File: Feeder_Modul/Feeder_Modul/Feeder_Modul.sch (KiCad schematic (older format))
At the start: 99 parts, among them J1 Conn_02x01, J101 Conn_02x01, J102 Conn_01x06_Male, J103 Conn_02x01, J104 Conn_02x01, J105 Conn_02x01, J106 USB_A, J107 Conn_02x07_Odd_Even, J108 Conn_02x01, J109 Conn_02x01, Q101 BC847, SW101 SW_Push, SW102 SW_Push, SW103 SW_Push, SW104 SW_Push, SW105 SW_Push, U1 TPS560430, U101 TPS560430, U102 STM32F105R8Tx, U103 M24C01-WMN, U104 EE-SX1350_PCB, U105 DRV8835, U107 SN65HVD230, Y101 48MHz

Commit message: Controller Modul geroutet
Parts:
- removed Q101: BC847, Package_TO_SOT_SMD:SOT-23, symbol Transistor_BJT:BC847
- removed R116: 10K, Resistor_SMD:R_0603_1608Metric, symbol Device:R_Small
- added D105: LED_Blue, LED_SMD:LED_0603_1608Metric, symbol Device:LED_Small
- J106: value USB_A -> WE_629104190121; footprint ProjectFootprints:USB-A-Conn_LCSC -> ProjectFootprints:WE629104190121; LCSC C46405 -> (none)
- R113: value 10K -> 1K; LCSC C99198 -> C21190
- R115: value 1k -> 10K; LCSC C21190 -> C99198
- U104: value EE-SX1350_PCB -> TCST5250; footprint ProjectFootprints:EE-SX1350_90deg -> ProjectFootprints:TCST5250; symbol PorjectLibrary:EE-SX1350_PCB -> PorjectLibrary:TCST5250
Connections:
- net +3V3: now also R115.2, D105.2 (A); no longer U104.4 (C)
- net ENC_OUT: now also R113.1, R115.1, U104.4 (C)
- net GND: now also U104.2 (C); no longer R113.2
- new net: D105.1 (K), R113.2
- no-connect marks 23 -> 21
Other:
- moved on the sheet: R109, R113
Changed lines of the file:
@@
 Connection ~ 14700 3400
 $Comp
-L PorjectLibrary:EE-SX1350_PCB U104
+L PorjectLibrary:TCST5250 U104
 U 1 1 60136449
-P 9400 4750
-F 0 "U104" H 9225 5147 60  0000 C CNN
-F 1 "EE-SX1350_PCB" H 9225 5041 60  0000 C CNN
-F 2 "ProjectFootprints:EE-SX1350_90deg" H 9400 4750 60  0001 C CNN
-F 3 "https://www.mouser.de/datasheet/2/307/en-ee_sx1350-1076544.pdf" H 9400 4750 60  0001 C CNN
-	1    9400 4750
-	1    0    0    -1
-$EndComp
-$Comp
-L Transistor_BJT:BC847 Q101
-U 1 1 6013824A
-P 10400 4600
-F 0 "Q101" H 10591 4646 50  0000 L CNN
-F 1 "BC847" H 10591 4555 50  0000 L CNN
-F 2 "Package_TO_SOT_SMD:SOT-23" H 10600 4525 50  0001 L CIN
-F 3 "http://www.infineon.com/dgdl/Infineon-BC847SERIES_BC848SERIES_BC849SERIES_BC850SERIES-DS-v01_01-en.pdf?fileId=db3a304314dca389011541d4630a1657" H 10400 4600 50  0001 L CNN
-F 4 "C475630" H 10750 4450 50  0000 C CNN "LCSC"
-	1    10400 4600
-	1    0    0    -1
-$EndComp
-$Comp
-L Device:R_Small R113
-U 1 1 60138354
-P 9850 4300
-F 0 "R113" H 9791 4254 50  0000 R CNN
-F 1 "10K" H 9791 4345 50  0000 R CNN
-F 2 "Resistor_SMD:R_0603_1608Metric" H 9850 4300 50  0001 C CNN
-F 3 "~" H 9850 4300 50  0001 C CNN
-F 4 "C99198" H 9850 4300 50  0001 C CNN "LCSC"
-	1    9850 4300
-	-1   0    0    1
-$EndComp
-Wire Wire Line
-	9850 4400 9850 4600
-$Comp
-L Device:R_Small R115
-U 1 1 6013AC18
-P 10100 4600
-F 0 "R115" V 9904 4600 50  0000 C CNN
-F 1 "1k" V 9995 4600 50  0000 C CNN
-F 2 "Resistor_SMD:R_0603_1608Metric" H 10100 4600 50  0001 C CNN
-F 3 "~" H 10100 4600 50  0001 C CNN
-F 4 "C21190" H 10100 4600 50  0001 C CNN "LCSC"
-	1    10100 4600
-	0    1    1    0
-$EndComp
-$Comp
-L power:GND #PWR0134
-U 1 1 6013AD13
-P 9850 4200
-F 0 "#PWR0134" H 9850 3950 50  0001 C CNN
-F 1 "GND" H 9855 4027 50  0000 C CNN
-F 2 "" H 9850 4200 50  0001 C CNN
-F 3 "" H 9850 4200 50  0001 C CNN
-	1    9850 4200
-	-1   0    0    1
-$EndComp
-Connection ~ 9850 4600
-Wire Wire Line
-	9850 4600 9700 4600
-Wire Wire Line
-	9850 4600 10000 4600
-$Comp
-L power:+3V3 #PWR0135
-U 1 1 601423FC
-P 9850 4900
-F 0 "#PWR0135" H 9850 4750 50  0001 C CNN
-F 1 "+3V3" V 9865 5028 50  0000 L CNN
-F 2 "" H 9850 4900 50  0001 C CNN
-F 3 "" H 9850 4900 50  0001 C CNN
-	1    9850 4900
-	0    1    1    0
-$EndComp
-Wire Wire Line
-	9850 4900 9700 4900
-$Comp
-L power:GND #PWR0138
-U 1 1 60144C45
-P 10500 5050
-F 0 "#PWR0138" H 10500 4800 50  0001 C CNN
-F 1 "GND" H 10505 4877 50  0000 C CNN
-F 2 "" H 10500 5050 50  0001 C CNN
-F 3 "" H 10500 5050 50  0001 C CNN
-	1    10500 5050
-	1    0    0    -1
-$EndComp
-Wire Wire Line
-	10500 5050 10500 4800
+P 8200 5250
+F 0 "U104" H 8025 5647 60  0000 C CNN
+F 1 "TCST5250" H 8025 5541 60  0000 C CNN
+F 2 "ProjectFootprints:TCST5250" H 8200 5250 60  0001 C CNN
+F 3 "https://www.mouser.de/datasheet/2/307/en-ee_sx1350-1076544.pdf" H 8200 5250 60  0001 C CNN
+	1    8200 5250
+	1    0    0    -1
+$EndComp
+Wire Wire Line
+	6950 4450 6950 4650
 $Comp
 L power:+3V3 #PWR0137
 U 1 1 6014609C
-P 10500 4000
-F 0 "#PWR0137" H 10500 3850 50  0001 C CNN
-F 1 "+3V3" H 10515 4173 50  0000 C CNN
-F 2 "" H 10500 4000 50  0001 C CNN
-F 3 "" H 10500 4000 50  0001 C CNN
-	1    10500 4000
-	1    0    0    -1
-$EndComp
-$Comp
-L Device:R_Small R116
-U 1 1 6014615D
-P 10500 4100
-F 0 "R116" H 10441 4054 50  0000 R CNN
-F 1 "10K" H 10441 4145 50  0000 R CNN
-F 2 "Resistor_SMD:R_0603_1608Metric" H 10500 4100 50  0001 C CNN
-F 3 "~" H 10500 4100 50  0001 C CNN
-F 4 "C99198" H 10500 4100 50  0001 C CNN "LCSC"
-	1    10500 4100
-	-1   0    0    1
-$EndComp
-Wire Wire Line
-	10500 4200 10500 4300
-Text Label 10650 4300 0    50   ~ 0
+P 6950 4050
+F 0 "#PWR0137" H 6950 3900 50  0001 C CNN
+F 1 "+3V3" H 6965 4223 50  0000 C CNN
+F 2 "" H 6950 4050 50  0001 C CNN
+F 3 "" H 6950 4050 50  0001 C CNN
+	1    6950 4050
+	-1   0    0    -1
+$EndComp
+Text Label 6700 4650 2    50   ~ 0
 ENC_OUT
-Wire Wire Line
-	10650 4300 10500 4300
-Connection ~ 10500 4300
-Wire Wire Line
-	10500 4300 10500 4400
 $Comp
 L Device:R_Small R109
 U 1 1 6014909F
-P 8400 4600
-F 0 "R109" V 8204 4600 50  0000 C CNN
-F 1 "1k" V 8295 4600 50  0000 C CNN
-F 2 "Resistor_SMD:R_0603_1608Metric" H 8400 4600 50  0001 C CNN
-F 3 "~" H 8400 4600 50  0001 C CNN
-F 4 "C21190" H 8400 4600 50  0001 C CNN "LCSC"
-	1    8400 4600
+P 7850 4000
+F 0 "R109" V 7654 4000 50  0000 C CNN
+F 1 "1k" V 7745 4000 50  0000 C CNN
+F 2 "Resistor_SMD:R_0603_1608Metric" H 7850 4000 50  0001 C CNN
+F 3 "~" H 7850 4000 50  0001 C CNN
+F 4 "C21190" H 7850 4000 50  0001 C CNN "LCSC"
+	1    7850 4000
 	0    1    1    0
 $EndComp
 Wire Wire Line
-	8750 4600 8500 4600
+	8000 4000 7950 4000
 $Comp
 L power:+3V3 #PWR0129
 U 1 1 6014A83A
-P 8050 4600
-F 0 "#PWR0129" H 8050 4450 50  0001 C CNN
-F 1 "+3V3" V 8065 4728 50  0000 L CNN
-F 2 "" H 8050 4600 50  0001 C CNN
-F 3 "" H 8050 4600 50  0001 C CNN
-	1    8050 4600
-	0    -1   -1   0
-$EndComp
-Wire Wire Line
-	8300 4600 8050 4600
+P 7700 3550
+F 0 "#PWR0129" H 7700 3400 50  0001 C CNN
+F 1 "+3V3" V 7715 3678 50  0000 L CNN
+F 2 "" H 7700 3550 50  0001 C CNN
+F 3 "" H 7700 3550 50  0001 C CNN
+	1    7700 3550
+	1    0    0    -1
+$EndComp
+Wire Wire Line
+	7750 4000 7700 4000
 $Comp
 L power:GND #PWR0128
 U 1 1 6014C039
-P 8000 4900
-F 0 "#PWR0128" H 8000 4650 50  0001 C CNN
-F 1 "GND" V 8005 4772 50  0000 R CNN
-F 2 "" H 8000 4900 50  0001 C CNN
-F 3 "" H 8000 4900 50  0001 C CNN
-	1    8000 4900
+P 7750 4150
+F 0 "#PWR0128" H 7750 3900 50  0001 C CNN
+F 1 "GND" V 7900 4150 50  0000 R CNN
+F 2 "" H 7750 4150 50  0001 C CNN
+F 3 "" H 7750 4150 50  0001 C CNN
+	1    7750 4150
 	0    1    1    0
 $EndComp
-Wire Wire Line
-	8750 4900 8000 4900
-NoConn ~ 8750 4750
-NoConn ~ 9700 4750
 Text Notes 14350 8350 0    50   ~ 0
 Feeder Steckplatz
@@
 P 14500 6100
 F 0 "J106" H 14555 6567 50  0000 C CNN
-F 1 "USB_A" H 14555 6476 50  0000 C CNN
-F 2 "ProjectFootprints:USB-A-Conn_LCSC" H 14650 6050 50  0001 C CNN
+F 1 "WE_629104190121" H 14555 6476 50  0000 C CNN
+F 2 "ProjectFootprints:WE629104190121" H 14650 6050 50  0001 C CNN
 F 3 "https://datasheet.lcsc.com/szlcsc/1811170208_Jing-Extension-of-the-Electronic-Co-LCSC-A-F90-Vinyl-Not-high-temperature_C46405.pdf" H 14650 6050 50  0001 C CNN
-F 4 "C46405" H 14550 6650 50  0000 C CNN "LCSC"
 	1    14500 6100
 	-1   0    0    -1
@@
 Text Notes 9100 5400 0    50   ~ 0
 Vishay Semiconductors\nCST5250
+Wire Wire Line
+	7700 3550 7700 4000
+Wire Wire Line
+	8000 4150 7750 4150
+$Comp
+L power:GND #PWR0134
+U 1 1 604E036D
+P 6700 4750
+F 0 "#PWR0134" H 6700 4500 50  0001 C CNN
+F 1 "GND" V 6705 4622 50  0000 R CNN
+F 2 "" H 6700 4750 50  0001 C CNN
+F 3 "" H 6700 4750 50  0001 C CNN
+	1    6700 4750
+	0    1    1    0
+$EndComp
+Wire Wire Line
+	6700 4750 8000 4750
+$Comp
+L Device:R_Small R113
+U 1 1 60138354
+P 6950 4350
+F 0 "R113" H 7250 4300 50  0000 R CNN
+F 1 "1K" H 7150 4400 50  0000 R CNN
+F 2 "Resistor_SMD:R_0603_1608Metric" H 6950 4350 50  0001 C CNN
+F 3 "~" H 6950 4350 50  0001 C CNN
+F 4 "C21190" H 6950 4350 50  0001 C CNN "LCSC"
+	1    6950 4350
+	1    0    0    1
+$EndComp
+Wire Wire Line
+	6950 4650 6800 4650
+Connection ~ 6950 4650
+$Comp
+L Device:LED_Small D105
+U 1 1 60570A78
+P 6950 4150
+F 0 "D105" V 7000 3950 50  0000 C CNN
+F 1 "LED_Blue" V 6900 3850 50  0000 C CNN
+F 2 "LED_SMD:LED_0603_1608Metric" V 6950 4150 50  0001 C CNN
+F 3 "https://datasheet.lcsc.com/szlcsc/TOGIALED-TJ-S1608SW6TGLC6B-A5_C192317.pdf" V 6950 4150 50  0001 C CNN
+F 4 "C192317" H 6950 4150 50  0001 C CNN "LCSC"
+	1    6950 4150
+	0    -1   -1   0
+$EndComp
+Wire Wire Line
+	6950 4650 8000 4650
+$Comp
+L Device:R_Small R115
+U 1 1 6017D48A
+P 6800 4350
+F 0 "R115" H 6741 4304 50  0000 R CNN
+F 1 "10K" H 6741 4395 50  0000 R CNN
+F 2 "Resistor_SMD:R_0603_1608Metric" H 6800 4350 50  0001 C CNN
+F 3 "~" H 6800 4350 50  0001 C CNN
+F 4 "C99198" H 6800 4350 50  0001 C CNN "LCSC"
+	1    6800 4350
+	1    0    0    1
+$EndComp
+Wire Wire Line
+	6800 4250 6800 4050
+Wire Wire Line
+	6800 4050 6950 4050
+Connection ~ 6950 4050
+Wire Wire Line
+	6800 4450 6800 4650
+Connection ~ 6800 4650
+Wire Wire Line
+	6800 4650 6700 4650
 $EndSCHEMATC

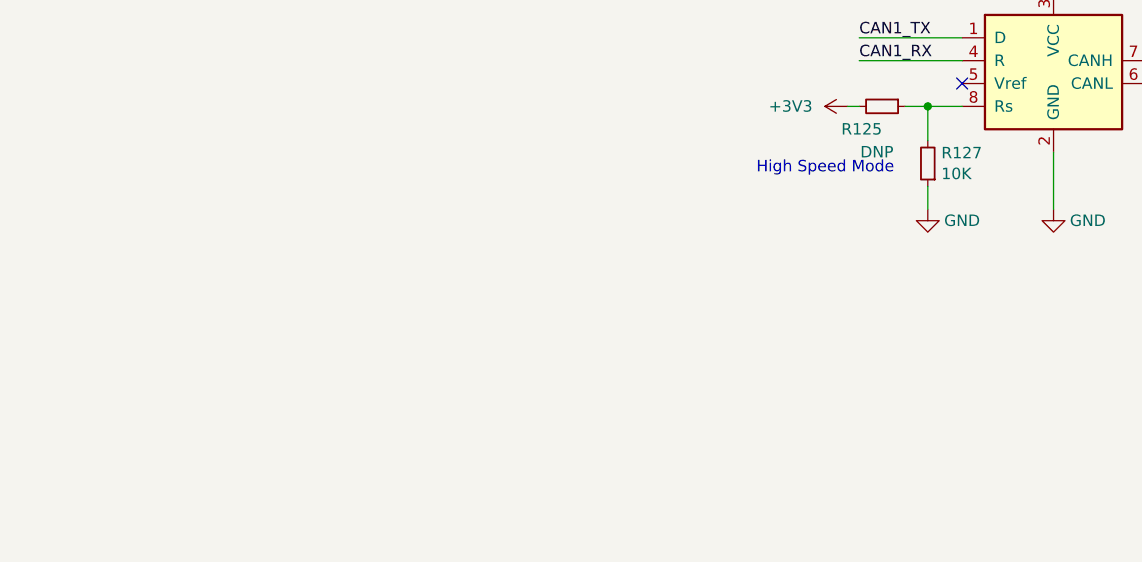
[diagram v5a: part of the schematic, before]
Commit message: Leere Symbole mit leeren Footprints hinzugefügt für BOM export
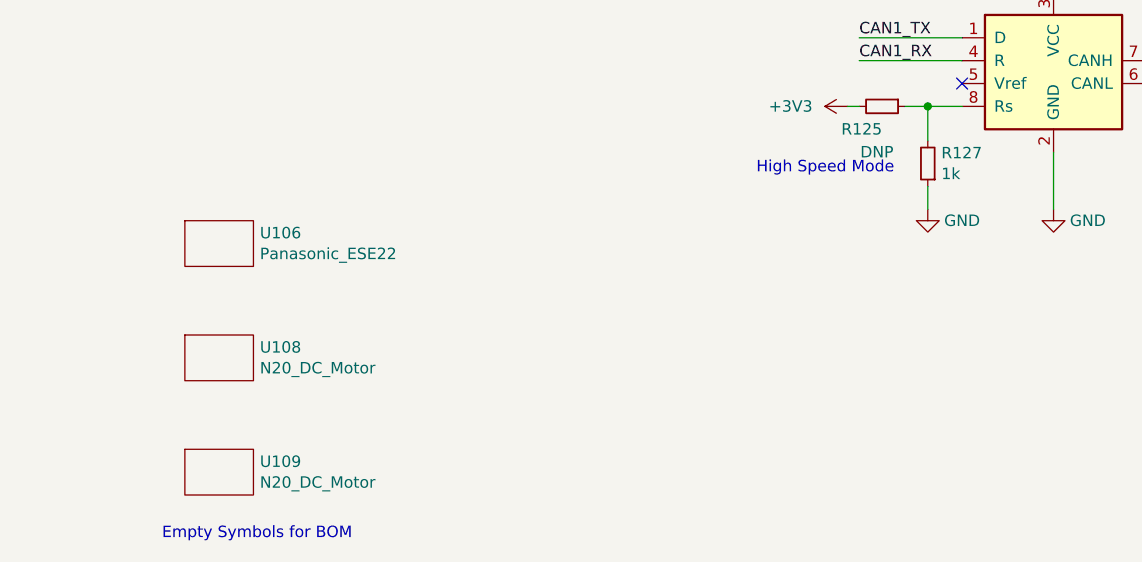
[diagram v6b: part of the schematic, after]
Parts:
- added U106: Panasonic_ESE22, ProjectFootprints:Empty, symbol PorjectLibrary:Empty
- added U108, U109: N20_DC_Motor, ProjectFootprints:Empty, symbol PorjectLibrary:Empty
- J106: LCSC (none) -> C718026
- J107: LCSC (none) -> C146608
- R127: value 10K -> 1k; LCSC C99198 -> C21190
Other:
- note added: "Empty Symbols for BOM"
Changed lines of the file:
@@
 F 2 "Connector_PinHeader_2.54mm:PinHeader_2x07_P2.54mm_Horizontal" H 14600 9000 50  0001 C CNN
 F 3 "~" H 14600 9000 50  0001 C CNN
+F 4 "C146608" H 14600 9000 50  0001 C CNN "LCSC"
 	1    14600 9000
 	1    0    0    -1
@@
 F 2 "ProjectFootprints:WE629104190121" H 14650 6050 50  0001 C CNN
 F 3 "https://datasheet.lcsc.com/szlcsc/1811170208_Jing-Extension-of-the-Electronic-Co-LCSC-A-F90-Vinyl-Not-high-temperature_C46405.pdf" H 14650 6050 50  0001 C CNN
+F 4 "C718026" H 14500 6100 50  0001 C CNN "LCSC"
 	1    14500 6100
 	-1   0    0    -1
@@
 P 10250 9250
 F 0 "R127" H 10191 9204 50  0000 R CNN
-F 1 "10K" H 10191 9295 50  0000 R CNN
+F 1 "1k" H 10191 9295 50  0000 R CNN
 F 2 "Resistor_SMD:R_0603_1608Metric" H 10250 9250 50  0001 C CNN
 F 3 "~" H 10250 9250 50  0001 C CNN
-F 4 "C99198" H 10250 9250 50  0001 C CNN "LCSC"
+F 4 "C21190" H 10250 9250 50  0001 C CNN "LCSC"
 	1    10250 9250
 	-1   0    0    1
@@
 Wire Wire Line
 	6800 4650 6700 4650
+$Comp
+L PorjectLibrary:Empty U106
+U 1 1 601D655D
+P 7150 9600
+F 0 "U106" H 7328 9646 50  0000 L CNN
+F 1 "Panasonic_ESE22" H 7328 9555 50  0000 L CNN
+F 2 "ProjectFootprints:Empty" H 7150 9600 50  0001 C CNN
+F 3 "" H 7150 9600 50  0001 C CNN
+	1    7150 9600
+	1    0    0    -1
+$EndComp
+$Comp
+L PorjectLibrary:Empty U108
+U 1 1 602321B1
+P 7150 10100
+F 0 "U108" H 7328 10146 50  0000 L CNN
+F 1 "N20_DC_Motor" H 7328 10055 50  0000 L CNN
+F 2 "ProjectFootprints:Empty" H 7150 10100 50  0001 C CNN
+F 3 "" H 7150 10100 50  0001 C CNN
+	1    7150 10100
+	1    0    0    -1
+$EndComp
+$Comp
+L PorjectLibrary:Empty U109
+U 1 1 60254EDC
+P 7150 10600
+F 0 "U109" H 7328 10646 50  0000 L CNN
+F 1 "N20_DC_Motor" H 7328 10555 50  0000 L CNN
+F 2 "ProjectFootprints:Empty" H 7150 10600 50  0001 C CNN
+F 3 "" H 7150 10600 50  0001 C CNN
+	1    7150 10600
+	1    0    0    -1
+$EndComp
+Text Notes 6900 10900 0    50   ~ 0
+Empty Symbols for BOM
 $EndSCHEMATC

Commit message: BOM für LCSC überarbeitet. Tool für BOM export modifiziert
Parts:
- C104, C105: LCSC C258467 -> C561171
- J102, L102, R103, R125, U104, U106, U108, U109: LCSC (none) -> 0
- R112: LCSC C384298 -> 0
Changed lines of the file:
@@
 F 2 "ProjectFootprints:TCST5250" H 8200 5250 60  0001 C CNN
 F 3 "https://www.mouser.de/datasheet/2/307/en-ee_sx1350-1076544.pdf" H 8200 5250 60  0001 C CNN
+F 4 "0" H 8200 5250 50  0001 C CNN "LCSC"
 	1    8200 5250
 	1    0    0    -1
@@
 F 2 "Capacitor_SMD:C_0603_1608Metric" H 2600 7000 50  0001 C CNN
 F 3 "~" H 2600 7000 50  0001 C CNN
-F 4 "C258467" V 2600 7000 50  0001 C CNN "LCSC"
+F 4 "C561171" V 2600 7000 50  0001 C CNN "LCSC"
 	1    2600 7000
 	0    1    1    0
@@
 F 2 "Capacitor_SMD:C_0603_1608Metric" H 2600 7300 50  0001 C CNN
 F 3 "~" H 2600 7300 50  0001 C CNN
-F 4 "C258467" V 2600 7300 50  0001 C CNN "LCSC"
+F 4 "C561171" V 2600 7300 50  0001 C CNN "LCSC"
 	1    2600 7300
 	0    1    1    0
@@
 F 2 "Resistor_SMD:R_0603_1608Metric" H 2950 6050 50  0001 C CNN
 F 3 "~" H 2950 6050 50  0001 C CNN
+F 4 "0" H 2950 6050 50  0001 C CNN "LCSC"
 	1    2950 6050
 	0    1    1    0
@@
 F 2 "Connector_PinHeader_2.54mm:PinHeader_1x06_P2.54mm_Horizontal" H 2600 10350 50  0001 C CNN
 F 3 "~" H 2600 10350 50  0001 C CNN
+F 4 "0" H 2600 10350 50  0001 C CNN "LCSC"
 	1    2600 10350
 	-1   0    0    -1
@@
 F 2 "ProjectFootprints:L_CommonModeChoke_Coilcraft_1812CAN" H 11650 8900 50  0001 C CNN
 F 3 "~" H 11650 8900 50  0001 C CNN
+F 4 "0" H 11650 8900 50  0001 C CNN "LCSC"
 	1    11650 8900
 	1    0    0    -1
@@
 F 2 "Resistor_SMD:R_0603_1608Metric" H 9700 1850 50  0001 C CNN
 F 3 "~" H 9700 1850 50  0001 C CNN
-F 4 "C384298" H 9700 1850 50  0001 C CNN "LCSC"
+F 4 "0" H 9700 1850 50  0001 C CNN "LCSC"
 	1    9700 1850
 	0    -1   -1   0
@@
 F 2 "Resistor_SMD:R_0603_1608Metric" H 10050 9000 50  0001 C CNN
 F 3 "~" H 10050 9000 50  0001 C CNN
+F 4 "0" H 10050 9000 50  0001 C CNN "LCSC"
 	1    10050 9000
 	0    1    1    0
@@
 F 2 "ProjectFootprints:Empty" H 7150 9600 50  0001 C CNN
 F 3 "" H 7150 9600 50  0001 C CNN
+F 4 "0" H 7150 9600 50  0001 C CNN "LCSC"
 	1    7150 9600
 	1    0    0    -1
@@
 F 2 "ProjectFootprints:Empty" H 7150 10100 50  0001 C CNN
 F 3 "" H 7150 10100 50  0001 C CNN
+F 4 "0" H 7150 10100 50  0001 C CNN "LCSC"
 	1    7150 10100
 	1    0    0    -1
@@
 F 2 "ProjectFootprints:Empty" H 7150 10600 50  0001 C CNN
 F 3 "" H 7150 10600 50  0001 C CNN
+F 4 "0" H 7150 10600 50  0001 C CNN "LCSC"
 	1    7150 10600
 	1    0    0    -1

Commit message: Feeder Rails hinzugefügt
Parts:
- J102: footprint Connector_PinHeader_2.54mm:PinHeader_1x06_P2.54mm_Horizontal -> Connector_PinHeader_2.54mm:PinHeader_1x06_P2.54mm_Vertical
- J107: footprint Connector_PinHeader_2.54mm:PinHeader_2x07_P2.54mm_Horizontal -> Connector_PinHeader_2.54mm:PinHeader_2x08_P2.54mm_Vertical; symbol Connector_Generic:Conn_02x07_Odd_Even -> Connector_Generic:Conn_02x08_Odd_Even; LCSC C146608 -> C9142
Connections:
- net ADDR0: now also J107.9 (Pin_9); no longer J107.7 (Pin_7)
- net ADDR1: now also J107.10 (Pin_10); no longer J107.8 (Pin_8)
- net ADDR2: now also J107.11 (Pin_11); no longer J107.9 (Pin_9)
- net ADDR3: now also J107.12 (Pin_12); no longer J107.10 (Pin_10)
- net ADDR4: now also J107.13 (Pin_13); no longer J107.11 (Pin_11)
- net ADDR5: now also J107.14 (Pin_14); no longer J107.12 (Pin_12)
- net ADDR6: now also J107.15 (Pin_15); no longer J107.13 (Pin_13)
- net ADDR7: now also J107.16 (Pin_16); no longer J107.14 (Pin_14)
- net CAN1_H: now also J107.3 (Pin_3), J107.4 (Pin_4); no longer J107.5 (Pin_5)
- net CAN1_L: now also J107.5 (Pin_5)
- net GND: now also J107.7 (Pin_7), J107.8 (Pin_8); no longer J107.3 (Pin_3), J107.4 (Pin_4)
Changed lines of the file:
@@
 	4650 9250 4550 9250
 $Comp
-L Connector_Generic:Conn_02x07_Odd_Even J107
+L Connector_Generic:Conn_02x08_Odd_Even J107
 U 1 1 6010A1B3
 P 14600 9000
 F 0 "J107" H 14650 9517 50  0000 C CNN
 F 1 "Conn_02x07_Odd_Even" H 14650 9426 50  0000 C CNN
-F 2 "Connector_PinHeader_2.54mm:PinHeader_2x07_P2.54mm_Horizontal" H 14600 9000 50  0001 C CNN
+F 2 "Connector_PinHeader_2.54mm:PinHeader_2x08_P2.54mm_Vertical" H 14600 9000 50  0001 C CNN
 F 3 "~" H 14600 9000 50  0001 C CNN
-F 4 "C146608" H 14600 9000 50  0001 C CNN "LCSC"
+F 4 "C9142" H 14600 9000 50  0001 C CNN "LCSC"
 	1    14600 9000
 	1    0    0    -1
@@
 L power:GND #PWR0142
 U 1 1 6010A872
-P 15600 8800
-F 0 "#PWR0142" H 15600 8550 50  0001 C CNN
-F 1 "GND" H 15605 8627 50  0000 C CNN
-F 2 "" H 15600 8800 50  0001 C CNN
-F 3 "" H 15600 8800 50  0001 C CNN
-	1    15600 8800
+P 15250 9000
+F 0 "#PWR0142" H 15250 8750 50  0001 C CNN
+F 1 "GND" H 15255 8827 50  0000 C CNN
+F 2 "" H 15250 9000 50  0001 C CNN
+F 3 "" H 15250 9000 50  0001 C CNN
+	1    15250 9000
 	1    0    0    -1
 $EndComp
 Wire Wire Line
-	15600 8800 14900 8800
-Text Label 14050 8900 0    50   ~ 0
+	15250 9000 14900 9000
+Text Label 14050 8800 0    50   ~ 0
 CAN1_H
 Text Label 15250 8900 2    50   ~ 0
@@
 	15250 8900 14900 8900
 Wire Wire Line
-	14050 8900 14400 8900
-Text Label 14400 9000 2    50   ~ 0
+	14050 8800 14400 8800
+Text Label 14400 9100 2    50   ~ 0
 ADDR0
-Text Label 14900 9000 0    50   ~ 0
+Text Label 14900 9100 0    50   ~ 0
 ADDR1
-Text Label 14400 9100 2    50   ~ 0
+Text Label 14400 9200 2    50   ~ 0
 ADDR2
-Text Label 14900 9100 0    50   ~ 0
+Text Label 14900 9200 0    50   ~ 0
 ADDR3
-Text Label 14400 9200 2    50   ~ 0
+Text Label 14400 9300 2    50   ~ 0
 ADDR4
-Text Label 14900 9200 0    50   ~ 0
+Text Label 14900 9300 0    50   ~ 0
 ADDR5
-Text Label 14400 9300 2    50   ~ 0
+Text Label 14400 9400 2    50   ~ 0
 ADDR6
-Text Label 14900 9300 0    50   ~ 0
+Text Label 14900 9400 0    50   ~ 0
 ADDR7
 Wire Wire Line
@@
 F 0 "J102" H 3000 10800 50  0000 C CNN
 F 1 "Conn_01x06_Male" H 2900 10700 50  0000 C CNN
-F 2 "Connector_PinHeader_2.54mm:PinHeader_1x06_P2.54mm_Horizontal" H 2600 10350 50  0001 C CNN
+F 2 "Connector_PinHeader_2.54mm:PinHeader_1x06_P2.54mm_Vertical" H 2600 10350 50  0001 C CNN
 F 3 "~" H 2600 10350 50  0001 C CNN
 F 4 "0" H 2600 10350 50  0001 C CNN "LCSC"
@@
 L power:GND #PWR0161
 U 1 1 601B6A88
-P 13700 8800
-F 0 "#PWR0161" H 13700 8550 50  0001 C CNN
-F 1 "GND" H 13705 8627 50  0000 C CNN
-F 2 "" H 13700 8800 50  0001 C CNN
-F 3 "" H 13700 8800 50  0001 C CNN
-	1    13700 8800
+P 14050 9000
+F 0 "#PWR0161" H 14050 8750 50  0001 C CNN
+F 1 "GND" H 14055 8827 50  0000 C CNN
+F 2 "" H 14050 9000 50  0001 C CNN
+F 3 "" H 14050 9000 50  0001 C CNN
+	1    14050 9000
 	-1   0    0    -1
 $EndComp
 Wire Wire Line
-	13700 8800 14400 8800
+	14050 9000 14400 9000
 $Comp
 L Connector_Generic:Conn_02x01 J?
@@
 Text Notes 6900 10900 0    50   ~ 0
 Empty Symbols for BOM
+Text Label 15250 8800 2    50   ~ 0
+CAN1_H
+Wire Wire Line
+	15250 8800 14900 8800
+Text Label 14050 8900 0    50   ~ 0
+CAN1_L
+Wire Wire Line
+	14050 8900 14400 8900
 $EndSCHEMATC
